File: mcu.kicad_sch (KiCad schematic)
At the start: 17 parts

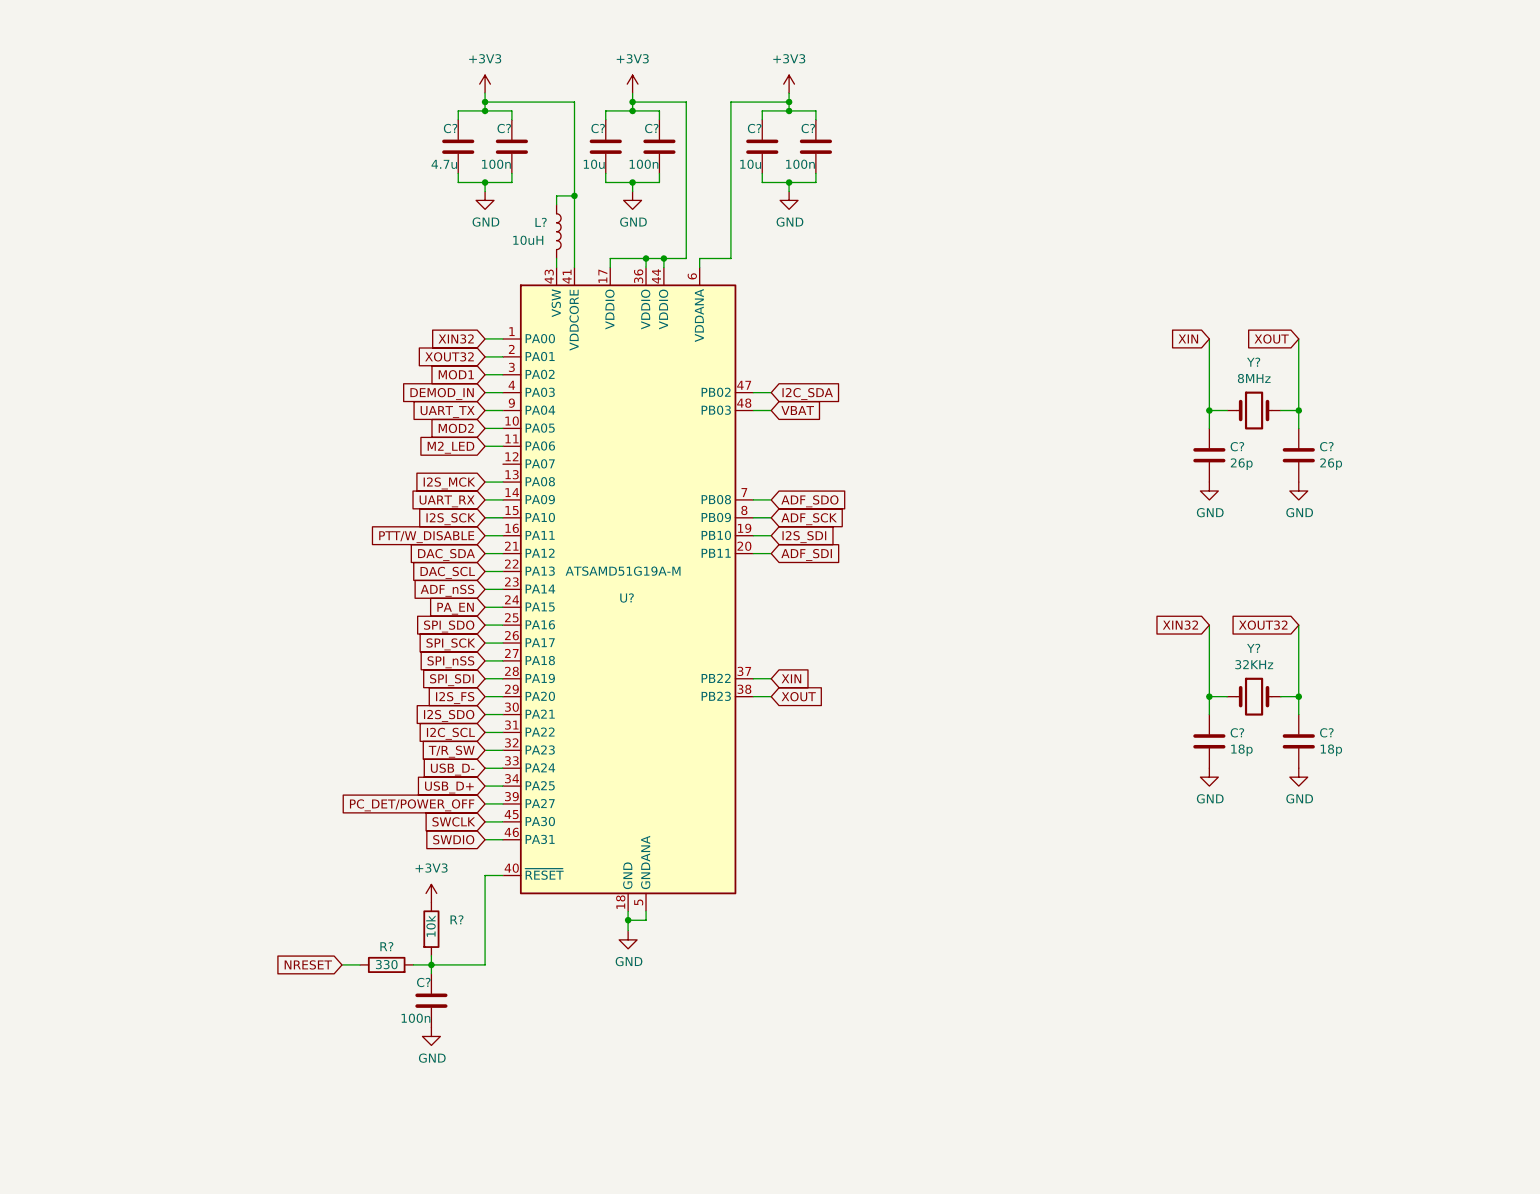
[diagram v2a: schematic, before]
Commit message: Schematic revision, details below.
[M.2 connector]
- Disconnected NRESET signal from pin 67 (RESET#_(O)_(O/1.8V)) as this would have caused a dangerous back-feed of 3.3V in a signal specified for 1.8V
- Moved I2S_FS signal to pin 26 to group it together the other I2S lines.
- Moved USART signals to pins 40 and 42.
- Moved I2C signals to pins 44 and 46.
- Replaced VBAT global label with '+BATT' power symbol.

[MCU]
- Replaced VBAT global label with '+BATT' global symbol.
- Added two more 100nF bypass capacitors for VDDIO pins.
- Removed wrong connection of VDDCORE to 3V3 power net.
- Connected 8MHz crystal directly to the corresponding pins, removed the global labels.
- Connected the 32kHz crystal directly to the corresponding pins, removed the global labels and changed its value to 32.768kHz.
- Changed the value of crystal load capacitors to 'TBD', as their value depends both on the chosen crystal and on PCB layout.
- Added notes for PCB routing.
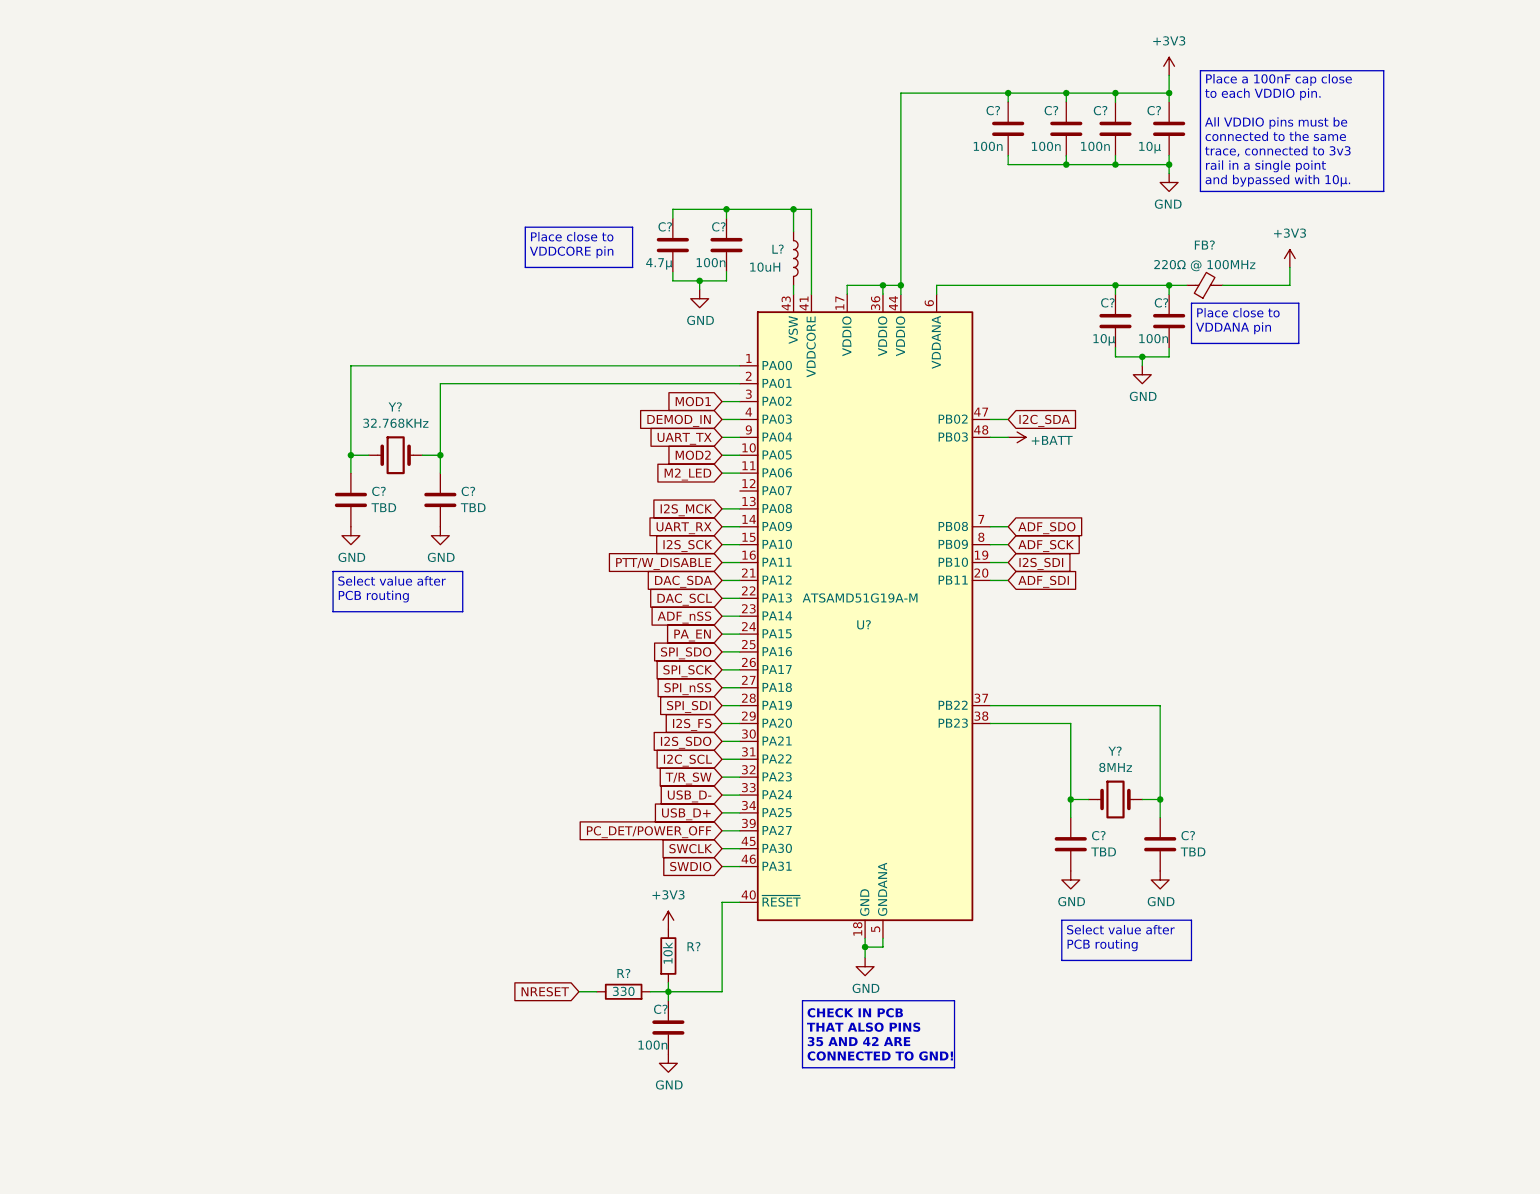
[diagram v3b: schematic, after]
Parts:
- added C? (x2): 100n, Capacitor_SMD:C_0402_1005Metric, symbol Device:C
- added FB?: 220Ω @ 100MHz, symbol Device:FerriteBead_Small
- C?: value 4.7u -> 4.7μ
- C? (x2): value 26p -> TBD
- C? (x2): value 18p -> TBD
- C? (x2): value 10u -> 10μ
- Y?: value 32KHz -> 32.768KHz
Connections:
- net +3V3: now also C?.1, C?.1, FB?.2; no longer C?.1, C?.1, C?.1, C?.1, L?.1, U?.41 (VDDCORE), U?.6 (VDDANA)
- net GND: now also C?.2, C?.2
- net VBAT renamed +BATT
- net XIN: no longer names the net of C?.1, Y?.1
- net XIN: now also U?.38 (PB23); no longer U?.37 (PB22)
- net XIN32: no longer names the net of C?.1, U?.1 (PA00), Y?.1
- net XOUT: no longer names the net of C?.1, Y?.2
- net XOUT: now also U?.37 (PB22); no longer U?.38 (PB23)
- net XOUT32: no longer names the net of C?.1, U?.2 (PA01), Y?.2
- new net: C?.1, C?.1, L?.1, U?.41 (VDDCORE)
- new net: C?.1, C?.1, FB?.1, U?.6 (VDDANA)
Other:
- note added: "CHECK IN PCB THAT ALSO PINS 35 AND 42 ARE CONNECTED TO GND!"
- note added: "Place a 100nF cap close to each VDDIO pin. All VDDIO pins must be connected to the same trace, connected to 3v3 rail in a single point and bypassed with 10μ."
- note added: "Place close to VDDANA pin"
- note added: "Place close to VDDCORE pin"
- note added: "Select value after PCB routing"
- moved on the sheet: C?, L?, R?, U?, Y?

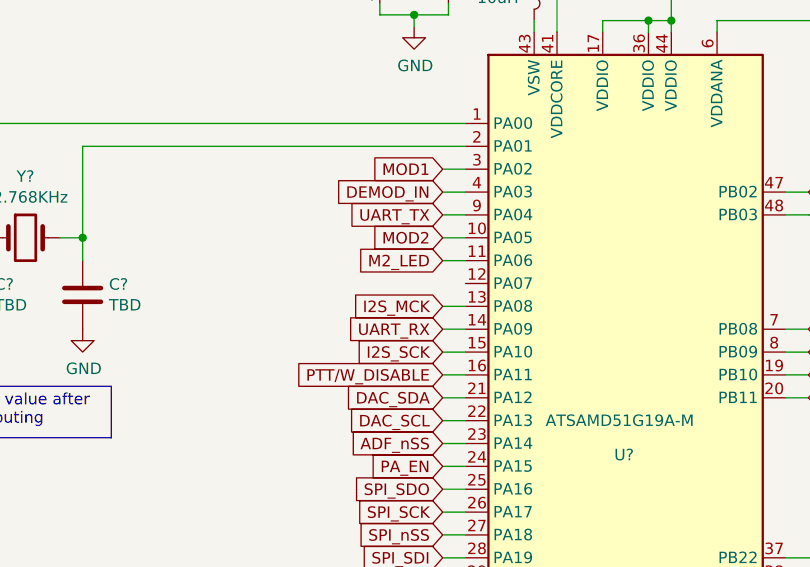
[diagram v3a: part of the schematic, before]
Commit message: Add MCU to ADF7021 connection
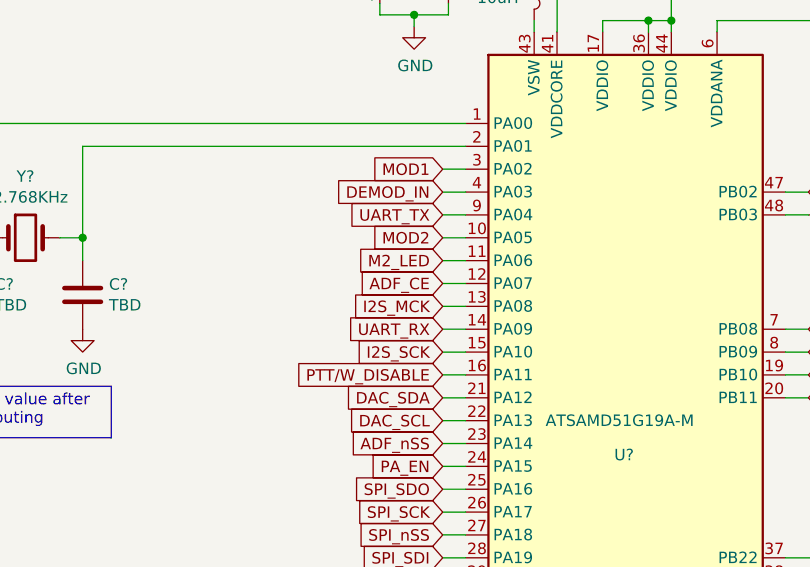
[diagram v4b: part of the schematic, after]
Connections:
- net ADF_CE: now reaches U?.12 (PA07)
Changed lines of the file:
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@@
+    (stroke (width 0) (type default) (color 0 0 0 0))
+  )
+  (wire (pts (xy 123.825 90.17) (xy 126.365 90.17))
     (stroke (width 0) (type default) (color 0 0 0 0))
   )
@@
     )
   )
+  (global_label "ADF_CE" (shape input) (at 123.825 90.17 180) (fields_autoplaced)
+    (effects (font (size 1.27 1.27)) (justify right))
+    (property "Intersheet References" "${INTERSHEET_REFS}" (id 0) (at 114.667 90.0906 0)
+      (effects (font (size 1.27 1.27)) (justify right) hide)
+    )
+  )

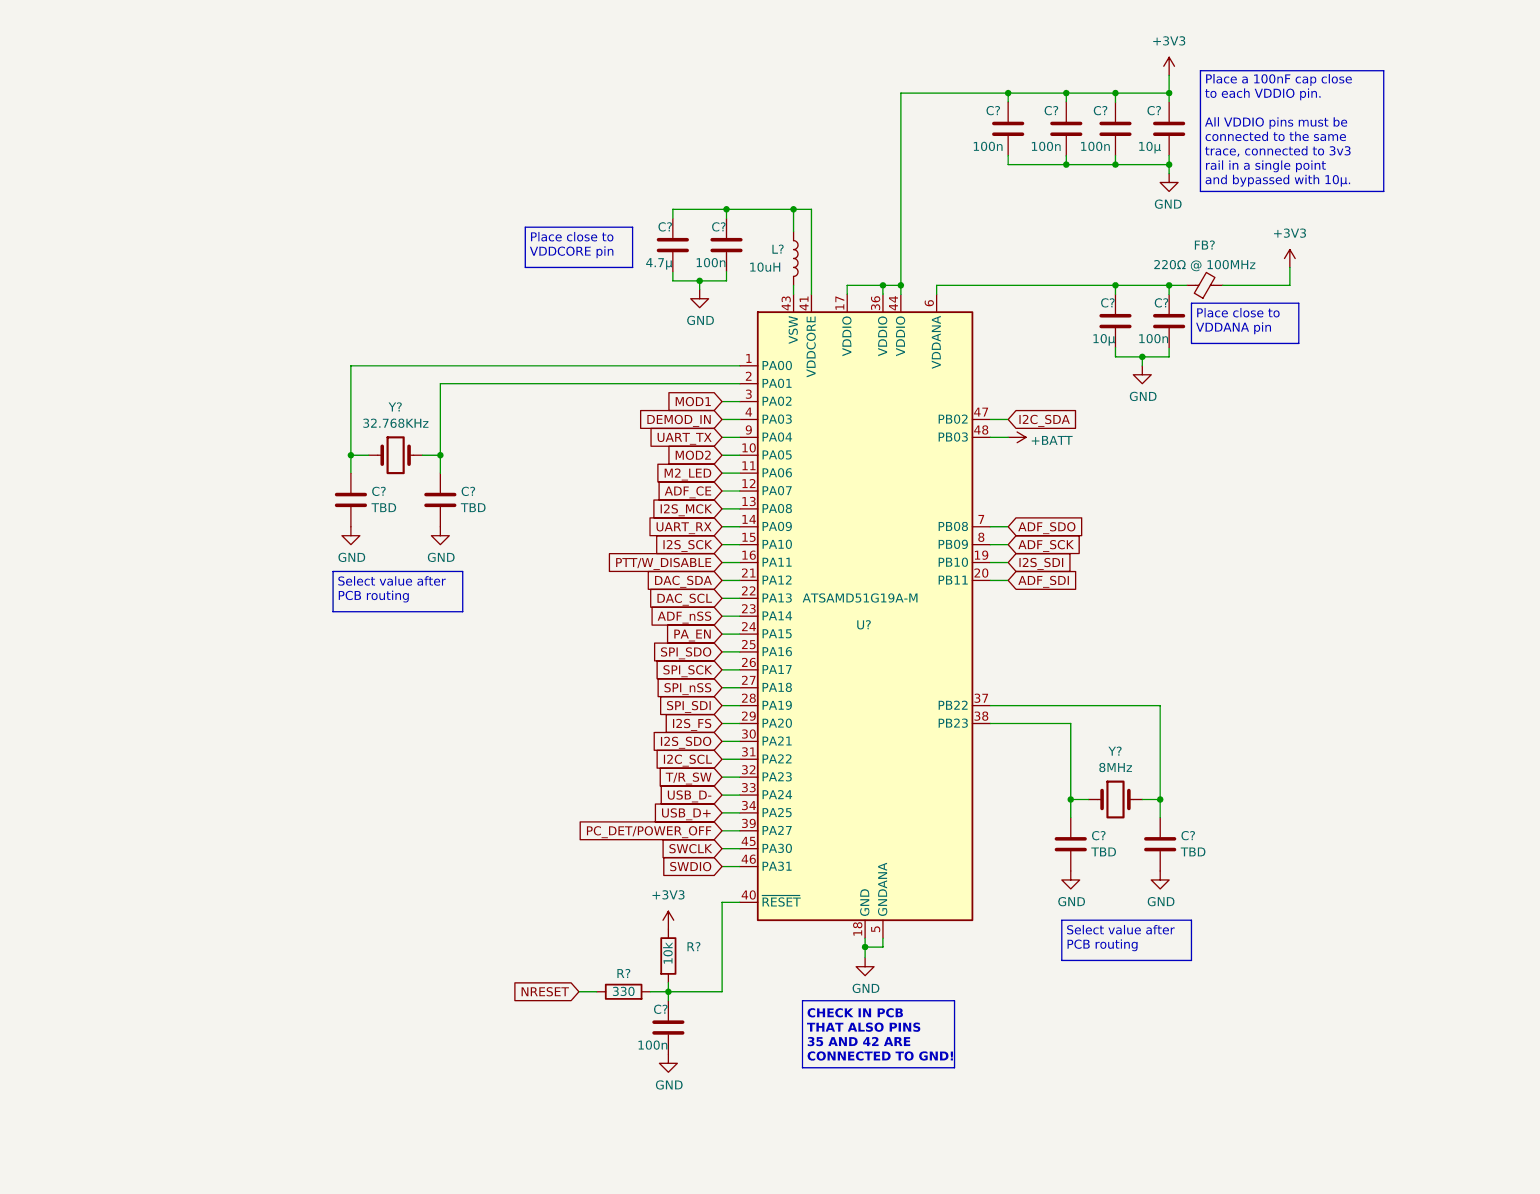
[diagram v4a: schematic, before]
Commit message: Added interfacing transistors for LED and nRESET signals on M.2 connector, switched from global to hierarchical net labels
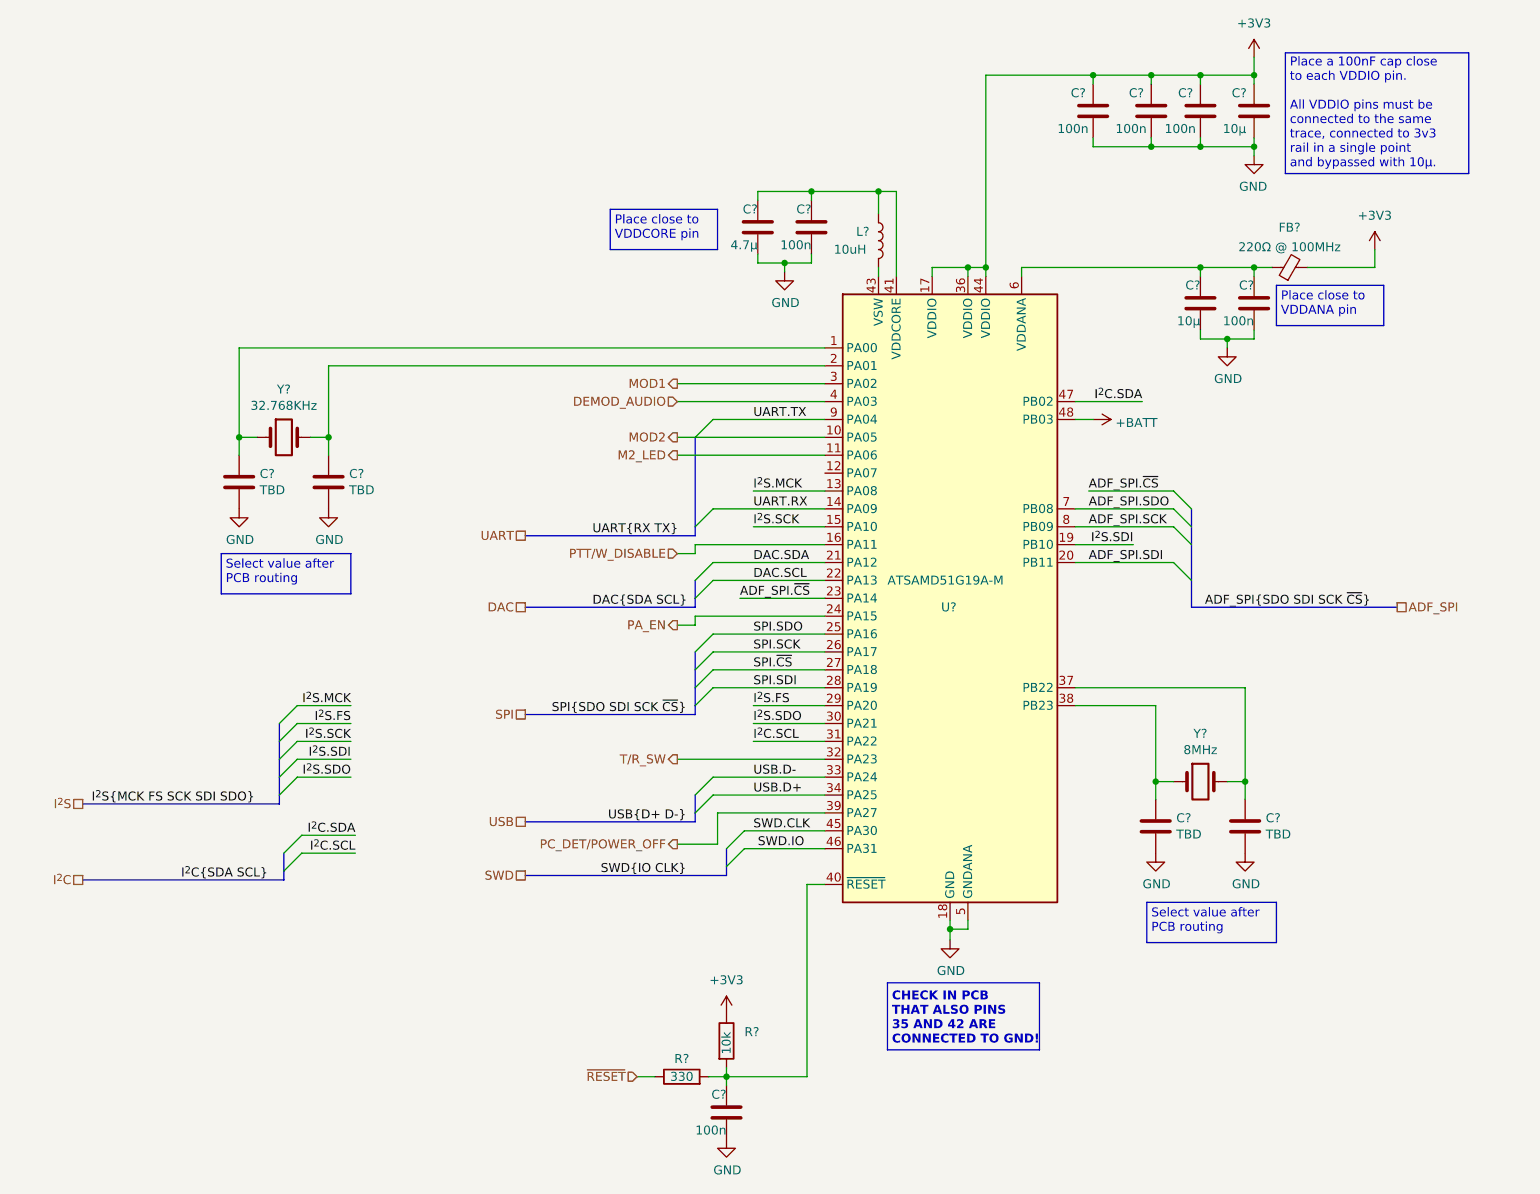
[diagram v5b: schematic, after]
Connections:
- net ADF_CE: no longer names the net of U?.12 (PA07)
- net ADF_SCK renamed ADF_SPI.SCK
- net ADF_SDI renamed ADF_SPI.SDI
- net ADF_SDO renamed ADF_SPI.SDO
- net ADF_nSS renamed ADF_SPI.~{CS}
- net DAC_SCL renamed DAC.SCL
- net DAC_SDA renamed DAC.SDA
- net DEMOD_IN renamed DEMOD_AUDIO
- net I2C_SCL renamed I^{2}C.SCL
- net I2C_SDA renamed I^{2}C.SDA
- net I2S_FS renamed I^{2}S.FS
- net I2S_MCK renamed I^{2}S.MCK
- net I2S_SCK renamed I^{2}S.SCK
- net I2S_SDI renamed I^{2}S.SDI
- net I2S_SDO renamed I^{2}S.SDO
- net NRESET renamed ~{RESET}
- net SPI_SCK renamed SPI.SCK
- net SPI_SDI renamed SPI.SDI
- net SPI_SDO renamed SPI.SDO
- net SPI_nSS renamed SPI.~{CS}
- net SWCLK renamed SWD.CLK
- net SWDIO renamed SWD.IO
- net UART_RX renamed UART.RX
- net UART_TX renamed UART.TX
- net USB_D+ renamed USB.D+
- net USB_D- renamed USB.D-
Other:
- company: (none) -> OpenRTX & M17
- title: (none) -> MCU
- moved on the sheet: C?, FB?, L?, R?, U?, Y?
